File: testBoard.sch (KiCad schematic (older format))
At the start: 75 parts, among them J1 Conn_02x05_Odd_Even, J2 Conn_01x06, J3 Conn_01x02, Q1 SCT2450KEC, SW1 PTS645SM43SMTR92_LFS, U1 PIC18F47K40, U10 INA233, U11 INA233, U12 TPS2557, U13 EMCO-Q50-5, U14 TPS2557, U15 EMCO-Q50-5, U16 MAX6675, U2 MAX6816, U3 WPMDM171050601, U4 WPMDM171050601, U5 MAX5483, U6 EMCO-Q10-5, U7 INA233, U8 INA233, U9 INA233

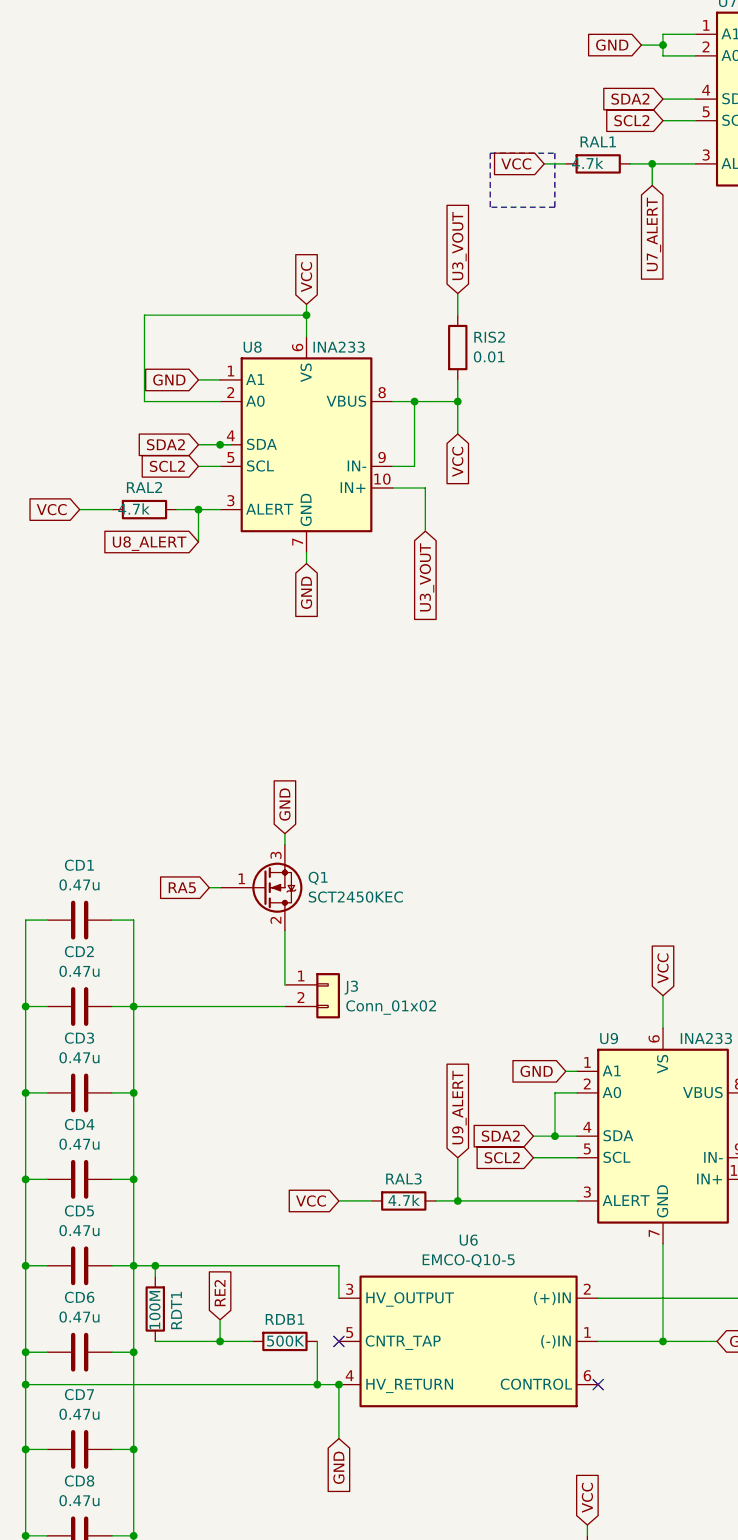
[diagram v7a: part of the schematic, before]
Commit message: Added some netlist names
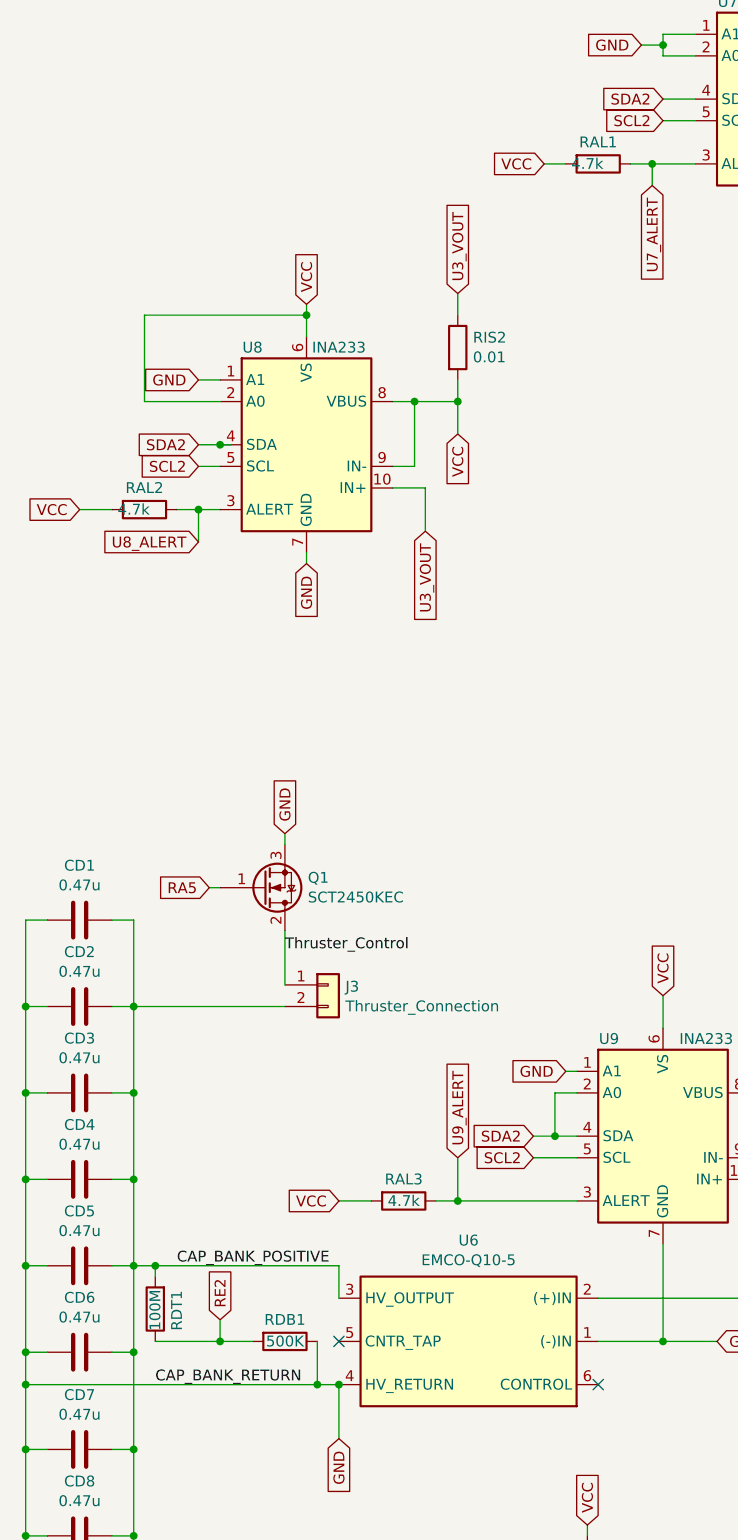
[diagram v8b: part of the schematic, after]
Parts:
- J3: value Conn_01x02 -> Thruster_Connection
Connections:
- net CAP_BANK_POSITIVE: now reaches CD1.1, CD10.1, CD11.1, CD12.1, CD2.1, CD3.1, CD4.1, CD5.1, CD6.1, CD7.1, CD8.1, CD9.1, J3.2 (Pin_2), RDT1.2, U6.3 (HV_OUTPUT)
- net Thruster_Control: now reaches J3.1 (Pin_1), Q1.2 (D)
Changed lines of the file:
@@
 P 1900 5400
 F 0 "J3" H 1980 5392 50  0000 L CNN
-F 1 "Conn_01x02" H 1980 5301 50  0000 L CNN
+F 1 "Thruster_Connection" H 1980 5301 50  0000 L CNN
 F 2 "PPTBoard:SolderWirePad_1x02_P0.220in_Drill0.110in" H 1900 5400 50  0001 C CNN
 F 3 "~" H 1900 5400 50  0001 C CNN
@@
 NoConn ~ 6600 9950
 NoConn ~ 6200 9950
-Text GLabel 2900 1600 0    50   Input ~ 0
-VCC
 Wire Wire Line
 	2900 1600 3000 1600
-Wire Notes Line
-	2650 1550 2950 1550
-Wire Notes Line
-	2950 1550 2950 1800
-Wire Notes Line
-	2950 1800 2650 1800
-Wire Notes Line
-	2650 1800 2650 1550
 $Comp
 L Device:C CD5
@@
 Wire Wire Line
 	1700 5400 1700 5150
+Text Label 1200 6700 0    50   ~ 0
+CAP_BANK_POSITIVE
+Text Label 1100 7250 0    50   ~ 0
+CAP_BANK_RETURN
+Text GLabel 2900 1600 0    50   Input ~ 0
+VCC
+Text Label 1700 5250 0    50   ~ 0
+Thruster_Control
 $EndSCHEMATC
